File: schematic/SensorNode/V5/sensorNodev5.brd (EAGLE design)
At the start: 66.9 x 87.7 mm, 35 parts, among them IC1 V_REG_MIC2920, J1 AVR_SPI_PRG_62X3_LOCK, U1 ATMEGA328P_TQFP, U2 ADA4077-1ARZ

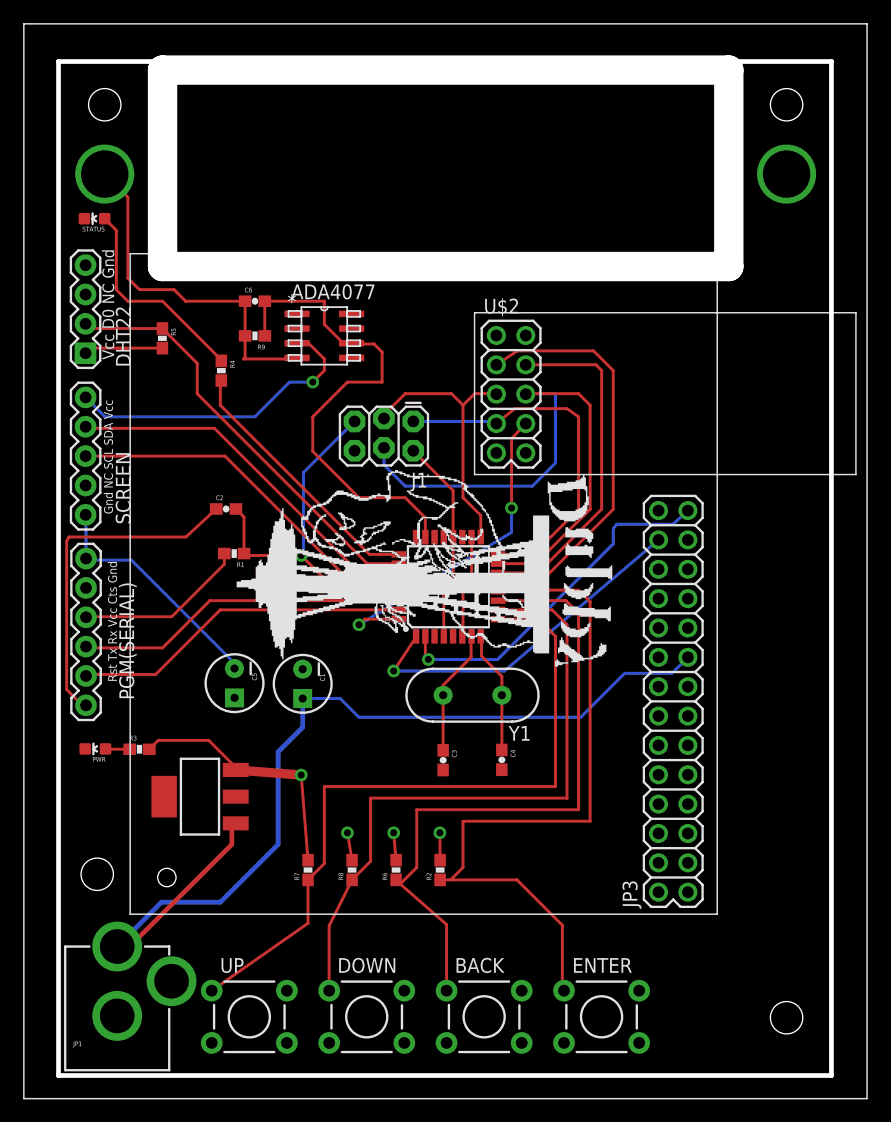
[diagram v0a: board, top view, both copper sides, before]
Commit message: o Updated Figaro gas sensor eagle part to reflect version A00 o Fixed opamp circuit in Sensor V5 o Swapped out DHT22 for Si7021
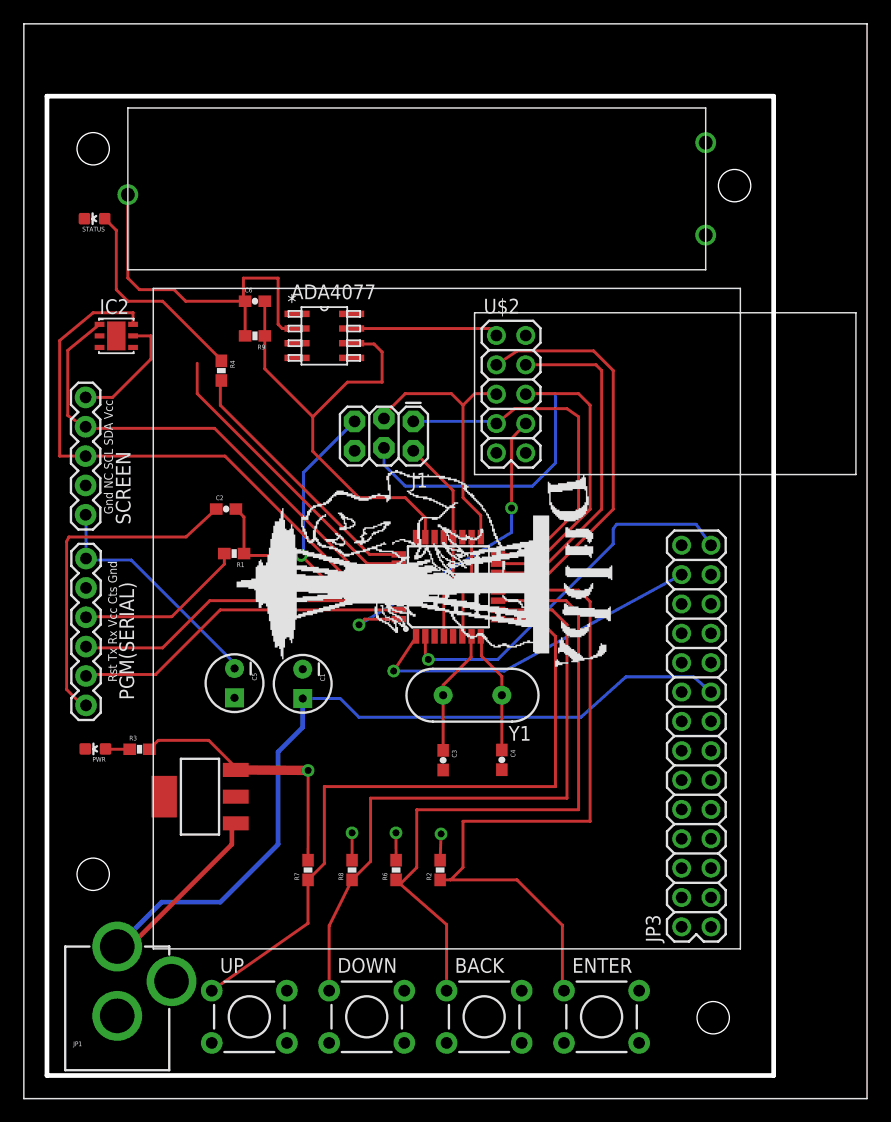
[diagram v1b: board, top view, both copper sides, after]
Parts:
- removed DHT22: (no value), SparkFun-Connectors:1X04
- removed R5: 4.7K, SparkFun-Resistors:0603-RES
- added IC2: SI7021-A10-GM, bespin:DFN6-3X3
- JP3: device misc:K-30 -> bespin:K-30
- moved U$1 55.7 mm to (6.00, 69.7), turned to 0 degrees
- moved JP3 3.61 mm to (59.0, 11.0)
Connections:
- net DTHP: no longer DHT22.2, R5.1
- net GND: now also IC2.2, U$1.CE1, U2.3, U2.4; no longer DHT22.4, U2.2, U2.7
- net N$12: now also U2.2; no longer U2.4
- net SCL: now also IC2.6
- net SDA: now also IC2.1
- net VCC: now also IC2.5, U2.7; no longer DHT22.1, R5.2, U2.3
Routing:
- net SCL: track 31.6 -> 52.1 mm
- net DTHP: track 37.2 -> 26.2 mm
- net SDA: track 32.3 -> 43.4 mm
- net VCC: track 106.3 -> 97.3 mm, vias 5 -> 4
- net TX_K30: track 30.7 -> 33.1 mm
- net 5V: track 82.8 -> 84.5 mm
- net N$12: track 30.5 -> 32.1 mm
- net ADA_OUT: track 42.8 -> 41.3 mm
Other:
- board size 66.9 x 87.7 mm -> 62.9 x 84.7 mm
- board text removed: "Vcc D0 NC Gnd"
